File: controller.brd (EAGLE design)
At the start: 56.8 x 64.8 mm, 30 parts, among them IC1 MEGA8-P, IC2 VREG-LM340, IC3 MAX6675, J1 ICSP, Q1 16.0Mhz

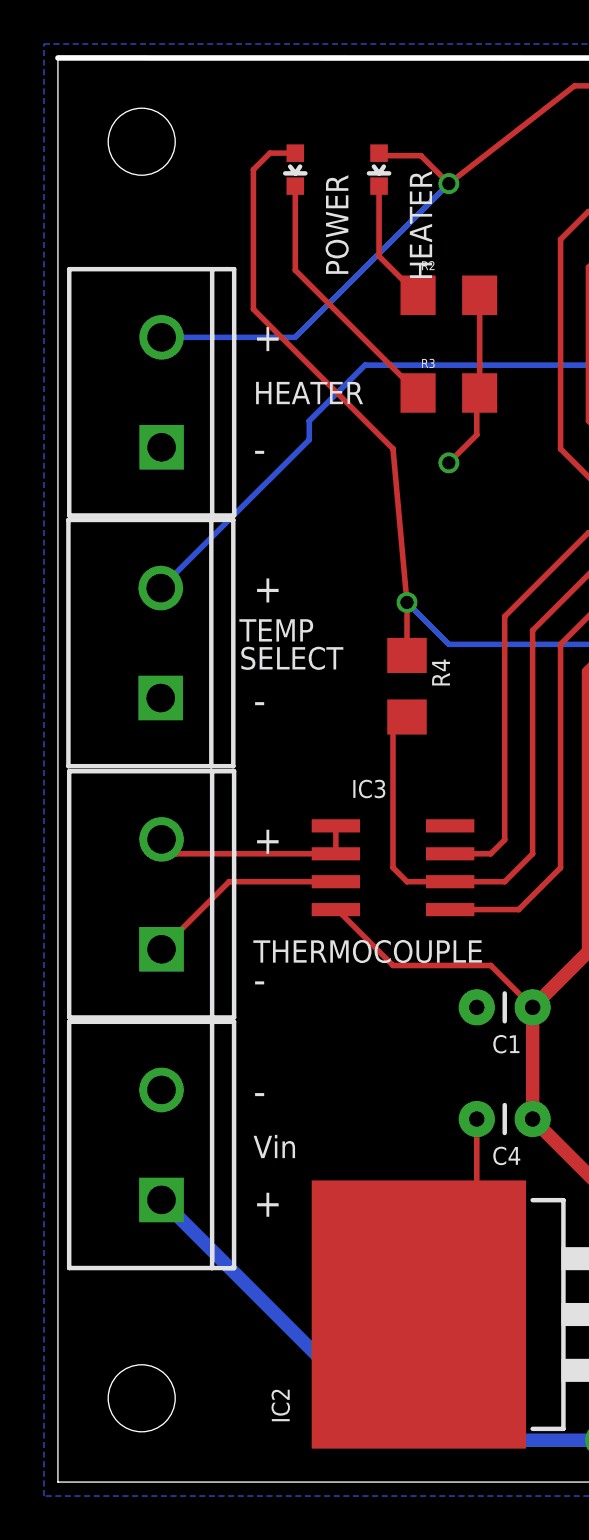
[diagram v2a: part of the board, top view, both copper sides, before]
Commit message: Silkscreen cleanup and terminal moves.
Silkscreen was overlapping the pad for Heater LED's
current limiting resitor.  Also spaced out screw terminals.
Prevents them from meshing but allows for use of different near
-equivalent parts.
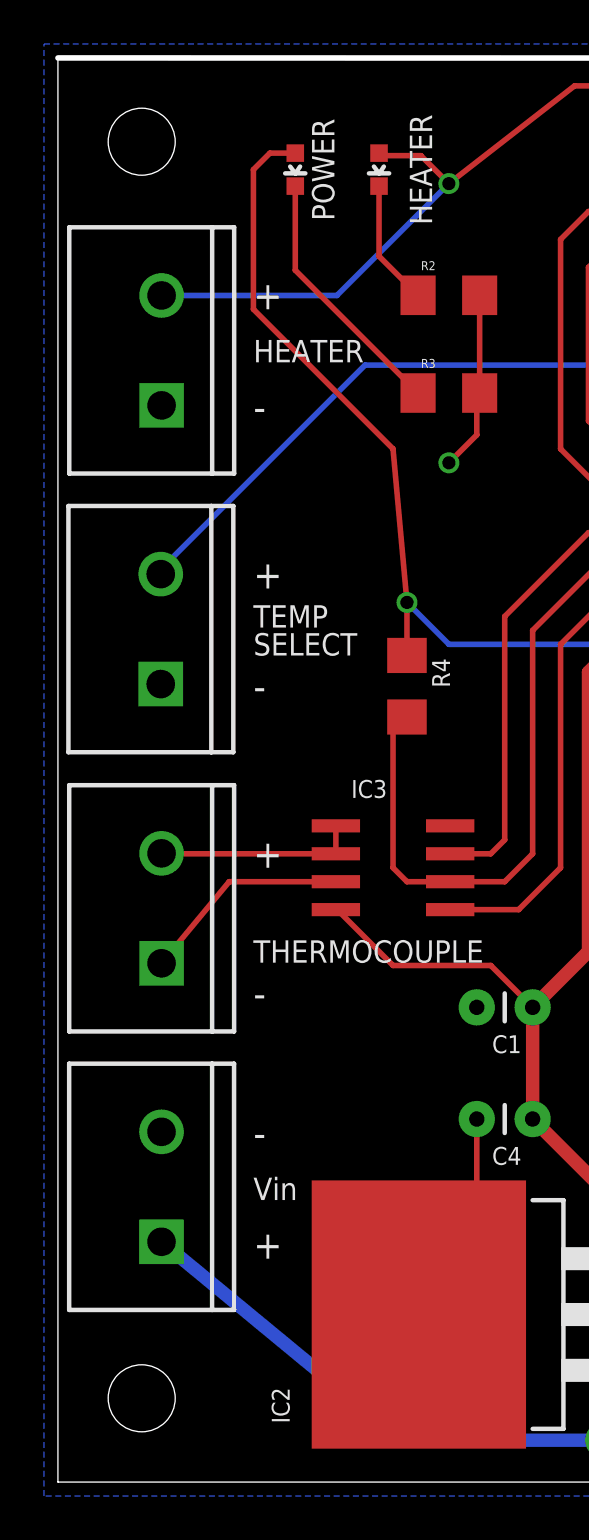
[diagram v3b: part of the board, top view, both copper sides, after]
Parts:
- moved JP2 1.91 mm to (4.71, 49.0)
- moved JP5 1.90 mm to (4.71, 10.9)
- moved JP4 0.64 mm to (4.68, 36.3)
- moved JP1 0.63 mm to (4.71, 23.6)
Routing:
- net 9VIN: track 28.6 -> 27.3 mm
- net HTR_OUT: track 50.6 -> 49.8 mm
- net SW_1: track 26.7 -> 26.1 mm
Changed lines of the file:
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@@
 <wire x1="56.82" y1="64.76" x2="0" y2="64.77" width="0.254" layer="20"/>
 <wire x1="0" y1="64.77" x2="0" y2="0" width="0" layer="20"/>
-<text x="8.89" y="49.53" size="1.016" layer="121" ratio="12" align="center-left">HEATER</text>
-<text x="8.255" y="38.735" size="1.016" layer="121" ratio="12" align="center-left">TEMP</text>
-<text x="8.255" y="37.465" size="1.016" layer="121" ratio="12" align="center-left">SELECT</text>
-<text x="8.89" y="15.24" size="1.016" layer="121" ratio="12" align="center-left">Vin</text>
-<text x="8.89" y="52.07" size="1.27" layer="121" ratio="12" align="center-left">+</text>
-<text x="8.89" y="40.64" size="1.27" layer="121" ratio="12" align="center-left">+</text>
-<text x="8.89" y="29.21" size="1.27" layer="121" ratio="12" align="center-left">+</text>
-<text x="8.89" y="12.7" size="1.27" layer="121" ratio="12" align="center-left">+</text>
-<text x="8.89" y="17.78" size="1.27" layer="121" ratio="12" align="center-left">-</text>
-<text x="8.89" y="22.86" size="1.27" layer="121" ratio="12" align="center-left">-</text>
-<text x="8.89" y="35.56" size="1.27" layer="121" ratio="12" align="center-left">-</text>
-<text x="8.89" y="46.99" size="1.27" layer="121" ratio="12" align="center-left">-</text>
-<text x="8.89" y="24.13" size="1.016" layer="121" ratio="12" align="center-left">THERMOCOUPLE</text>
-<text x="37.465" y="5.08" size="1.27" layer="121" ratio="12" rot="R90" align="center-left">SDA</text>
-<text x="34.925" y="5.08" size="1.27" layer="121" ratio="12" rot="R90" align="center-left">SCL</text>
-<text x="45.72" y="5.08" size="1.27" layer="121" ratio="12" rot="R90" align="center-left">TX</text>
-<text x="43.18" y="5.08" size="1.27" layer="121" ratio="12" rot="R90" align="center-left">RX</text>
-<text x="46.99" y="37.465" size="1.27" layer="121" ratio="12" align="center-right">+5V</text>
-<text x="46.99" y="34.925" size="1.27" layer="121" ratio="12" align="center-right">GND</text>
-<text x="16.51" y="57.15" size="1.016" layer="121" ratio="12" rot="R90" align="center">HEATER</text>
-<text x="12.7" y="57.15" size="1.016" layer="121" ratio="12" rot="R90" align="center">POWER</text>
-<text x="55.245" y="51.435" size="1.016" layer="121" ratio="12" rot="R90">REV 1.0</text>
+<text x="8.89" y="51.435" size="1.016" layer="25" ratio="12" align="center-left">HEATER</text>
+<text x="8.89" y="39.37" size="1.016" layer="25" ratio="12" align="center-left">TEMP</text>
+<text x="8.89" y="38.1" size="1.016" layer="25" ratio="12" align="center-left">SELECT</text>
+<text x="8.89" y="13.335" size="1.016" layer="25" ratio="12" align="center-left">Vin</text>
+<text x="8.89" y="53.975" size="1.27" layer="25" ratio="12" align="center-left">+</text>
+<text x="8.89" y="41.275" size="1.27" layer="25" ratio="12" align="center-left">+</text>
+<text x="8.89" y="28.575" size="1.27" layer="25" ratio="12" align="center-left">+</text>
+<text x="8.89" y="10.795" size="1.27" layer="25" ratio="12" align="center-left">+</text>
+<text x="8.89" y="15.875" size="1.27" layer="25" ratio="12" align="center-left">-</text>
+<text x="8.89" y="22.225" size="1.27" layer="25" ratio="12" align="center-left">-</text>
+<text x="8.89" y="36.195" size="1.27" layer="25" ratio="12" align="center-left">-</text>
+<text x="8.89" y="48.895" size="1.27" layer="25" ratio="12" align="center-left">-</text>
+<text x="8.89" y="24.13" size="1.016" layer="25" ratio="12" align="center-left">THERMOCOUPLE</text>
+<text x="37.465" y="5.08" size="1.27" layer="25" ratio="12" rot="R90" align="center-left">SDA</text>
+<text x="34.925" y="5.08" size="1.27" layer="25" ratio="12" rot="R90" align="center-left">SCL</text>
+<text x="45.72" y="5.08" size="1.27" layer="25" ratio="12" rot="R90" align="center-left">TX</text>
+<text x="43.18" y="5.08" size="1.27" layer="25" ratio="12" rot="R90" align="center-left">RX</text>
+<text x="46.99" y="37.465" size="1.27" layer="25" ratio="12" align="center-right">+5V</text>
+<text x="46.99" y="34.925" size="1.27" layer="25" ratio="12" align="center-right">GND</text>
+<text x="16.51" y="59.69" size="1.016" layer="25" ratio="12" rot="R90" align="center">HEATER</text>
+<text x="12.065" y="59.69" size="1.016" layer="25" ratio="12" rot="R90" align="center">POWER</text>
+<text x="55.245" y="51.435" size="1.016" layer="25" ratio="12" rot="R90">REV 1.0</text>
 </plain>
 <attributes>
@@
 <attribute name="NAME" x="21.082" y="20.32" size="0.8128" layer="25" rot="R180"/>
 </element>
-<element name="JP1" library="SparkFun-Connectors" package="SCREWTERMINAL-5MM-2" value="Thermocouple" x="4.712746875" y="24.229309375" smashed="yes" rot="R90"/>
-<element name="JP2" library="SparkFun-Connectors" package="SCREWTERMINAL-5MM-2" value="Heater" x="4.7147" y="47.062378125" smashed="yes" rot="R90"/>
+<element name="JP1" library="SparkFun-Connectors" package="SCREWTERMINAL-5MM-2" value="Thermocouple" x="4.712746875" y="23.594309375" smashed="yes" rot="R90"/>
+<element name="JP2" library="SparkFun-Connectors" package="SCREWTERMINAL-5MM-2" value="Heater" x="4.7147" y="48.967378125" smashed="yes" rot="R90"/>
 <element name="JP3" library="SparkFun-Connectors" package="2X5-SHROUDED_LOCK" value="M05X2SHD_LOCK" x="50.8" y="20.32" smashed="yes" rot="R180">
 <attribute name="NAME" x="53.721" y="31.242" size="0.4064" layer="104" rot="R180"/>
@@
 <attribute name="VALUE" x="24.765" y="58.42" size="1.016" layer="27" ratio="12" rot="R90" align="center"/>
 </element>
-<element name="JP4" library="SparkFun-Connectors" package="SCREWTERMINAL-5MM-2" value="Switch" x="4.676296875" y="35.658125" smashed="yes" rot="R90"/>
+<element name="JP4" library="SparkFun-Connectors" package="SCREWTERMINAL-5MM-2" value="Switch" x="4.676296875" y="36.293125" smashed="yes" rot="R90"/>
 <element name="IC3" library="SparkFun-AnalogIC" package="SO08-MAX6675" value="MAX6675" x="15.24" y="27.94" smashed="yes" rot="R270">
 <attribute name="NAME" x="13.335" y="31.115" size="0.8128" layer="25"/>
@@
 <attribute name="NAME" x="17.018" y="37.465" size="0.8128" layer="25" rot="R270"/>
 </element>
-<element name="JP5" library="SparkFun-Connectors" package="SCREWTERMINAL-5MM-2" value="Vin" x="4.71115" y="12.833065625" smashed="yes" rot="R90"/>
+<element name="JP5" library="SparkFun-Connectors" package="SCREWTERMINAL-5MM-2" value="Vin" x="4.71115" y="10.928065625" smashed="yes" rot="R90"/>
 <element name="R1" library="SparkFun-Resistors" package="1206" value="10kOhm" x="34.29" y="11.43" smashed="yes" rot="R90">
 <attribute name="NAME" x="33.147" y="10.16" size="0.4064" layer="25" rot="R90"/>
@@
 <contactref element="JP9" pad="1"/>
 <wire x1="12.64" y1="28.575" x2="5.36705625" y2="28.575" width="0.254" layer="1"/>
-<wire x1="5.36705625" y1="28.575" x2="4.712746875" y2="29.229309375" width="0.254" layer="1"/>
+<wire x1="5.36705625" y1="28.575" x2="4.712746875" y2="28.594309375" width="0.254" layer="1"/>
 </signal>
 <signal name="ICSP_RESET">
@@
 <wire x1="34.925" y1="62.23" x2="34.925" y2="51.435" width="0.254" layer="1"/>
 <wire x1="34.925" y1="51.435" x2="34.29" y2="50.8" width="0.254" layer="1"/>
-<wire x1="4.7147" y1="52.062378125" x2="10.787378125" y2="52.062378125" width="0.254" layer="16"/>
-<wire x1="10.787378125" y1="52.062378125" x2="17.78" y2="59.055" width="0.254" layer="16"/>
+<wire x1="17.78" y1="59.055" x2="12.692378125" y2="53.967378125" width="0.254" layer="16"/>
+<wire x1="12.692378125" y1="53.967378125" x2="4.7147" y2="53.967378125" width="0.254" layer="16"/>
 </signal>
 <signal name="TC+">
@@
 <contactref element="IC3" pad="3"/>
 <wire x1="12.64" y1="27.305" x2="7.7884375" y2="27.305" width="0.254" layer="1"/>
-<wire x1="7.7884375" y1="27.305" x2="4.712746875" y2="24.229309375" width="0.254" layer="1"/>
+<wire x1="7.7884375" y1="27.305" x2="4.712746875" y2="23.594309375" width="0.254" layer="1"/>
 </signal>
 <signal name="BTN1">
@@
 <contactref element="JP4" pad="2"/>
 <contactref element="IC1" pad="15"/>
-<wire x1="11.43" y1="48.26" x2="13.97" y2="50.8" width="0.254" layer="16"/>
 <wire x1="13.97" y1="50.8" x2="26.67" y2="50.8" width="0.254" layer="16"/>
-<wire x1="11.43" y1="48.26" x2="11.43" y2="47.402284375" width="0.254" layer="16"/>
-<wire x1="11.43" y1="47.402284375" x2="4.676296875" y2="40.658125" width="0.254" layer="16"/>
+<wire x1="13.97" y1="50.8" x2="4.676296875" y2="41.506296875" width="0.254" layer="16"/>
+<wire x1="4.676296875" y1="41.506296875" x2="4.676296875" y2="41.293125" width="0.254" layer="16"/>
 </signal>
 <signal name="N$1">
@@
 <wire x1="26.69" y1="3.79" x2="26.69" y2="5.08" width="0.6096" layer="1"/>
 <wire x1="24.805" y1="1.905" x2="15.639215625" y2="1.905" width="0.6096" layer="16"/>
-<wire x1="15.639215625" y1="1.905" x2="4.71115" y2="12.833065625" width="0.6096" layer="16"/>
+<wire x1="15.639215625" y1="1.905" x2="4.71115" y2="10.928065625" width="0.6096" layer="16"/>
 </signal>
 <signal name="XTAL2">

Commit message: Updated some layout, added logo
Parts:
- added U$1: MN-LOGO, Mikes-Aesthetics:MN-LOGO
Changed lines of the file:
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@@
 <element name="U$5" library="SparkFun-Electromechanical" package="STAND-OFF-TIGHT" value="" x="52.705" y="3.81" rot="R90"/>
 <element name="JP9" library="SparkFun-Connectors" package="MOLEX-1X2" value="PWR_AUX" x="53.975" y="34.925" smashed="yes" rot="R90"/>
+<element name="U$1" library="Mikes-Aesthetics" package="MN-LOGO" value="MN-LOGO" x="41.91" y="20.32" rot="MR270"/>
 </elements>
 <signals>
